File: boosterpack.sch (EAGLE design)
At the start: 27 parts, among them J1 POWERPOLE_DOUBLE

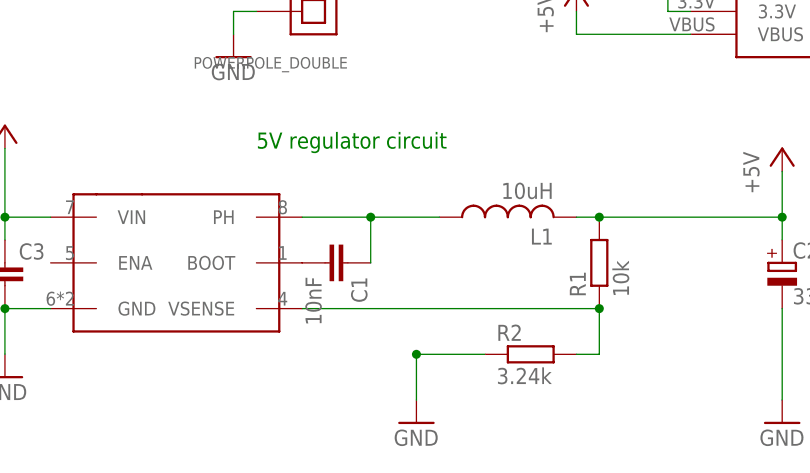
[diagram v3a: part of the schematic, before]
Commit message: added diode i forgot; routed new diode
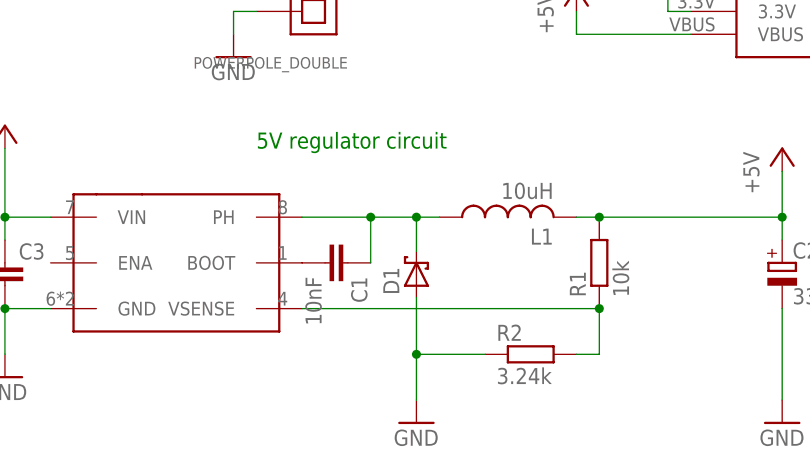
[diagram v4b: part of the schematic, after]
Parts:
- added D1: (no value), diode:SCHOTTKY-DIODEDO35-7
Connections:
- net GND: now also D1.A
- net N$11: now also D1.C
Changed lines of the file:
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@@
 <part name="GND7" library="supply1" deviceset="GND" device=""/>
 <part name="GND8" library="supply1" deviceset="GND" device=""/>
+<part name="D1" library="diode" deviceset="SCHOTTKY-DIODE" device="DO35-7"/>
 </parts>
 <sheets>
@@
 <instance part="GND7" gate="1" x="134.62" y="86.36"/>
 <instance part="GND8" gate="1" x="-2.54" y="73.66"/>
+<instance part="D1" gate="G$1" x="25.4" y="-3.81" rot="R90"/>
 </instances>
 <busses>
@@
 <wire x1="25.4" y1="-12.7" x2="25.4" y2="-17.78" width="0.1524" layer="91"/>
 <junction x="25.4" y="-12.7"/>
+<pinref part="D1" gate="G$1" pin="A"/>
+<wire x1="25.4" y1="-12.7" x2="25.4" y2="-6.35" width="0.1524" layer="91"/>
 </segment>
 <segment>
@@
 <wire x1="12.7" y1="2.54" x2="20.32" y2="2.54" width="0.1524" layer="91"/>
 <pinref part="C1" gate="G$1" pin="1"/>
-<wire x1="20.32" y1="2.54" x2="27.94" y2="2.54" width="0.1524" layer="91"/>
+<wire x1="20.32" y1="2.54" x2="25.4" y2="2.54" width="0.1524" layer="91"/>
+<wire x1="25.4" y1="2.54" x2="27.94" y2="2.54" width="0.1524" layer="91"/>
 <wire x1="20.32" y1="-2.54" x2="20.32" y2="2.54" width="0.1524" layer="91"/>
 <junction x="20.32" y="2.54"/>
-</segment>
-</net>
+<pinref part="D1" gate="G$1" pin="C"/>
+<wire x1="25.4" y1="-1.27" x2="25.4" y2="2.54" width="0.1524" layer="91"/>
+<junction x="25.4" y="2.54"/>
+</segment>
+</net>

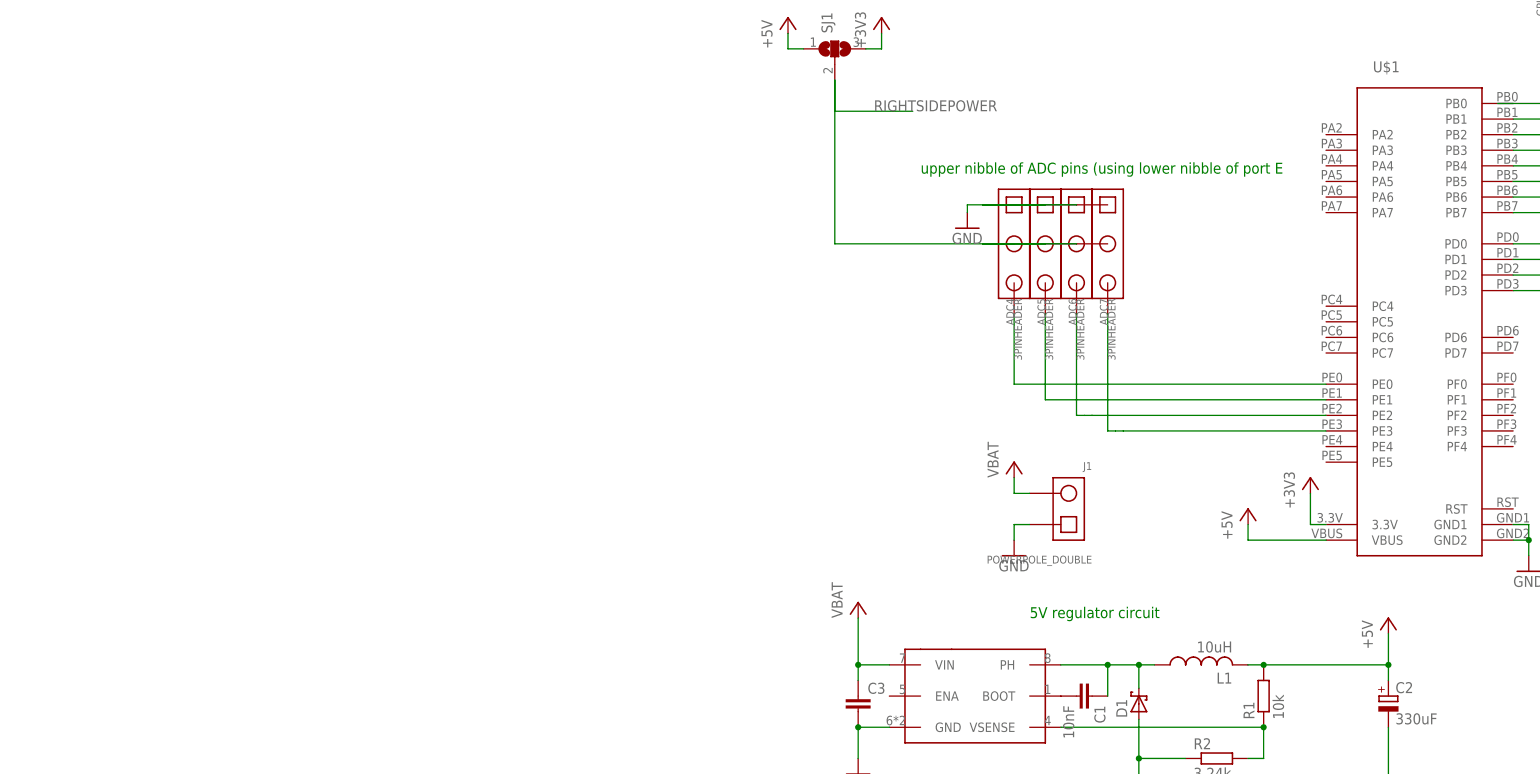
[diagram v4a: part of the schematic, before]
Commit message: added spi motor driver for two motors
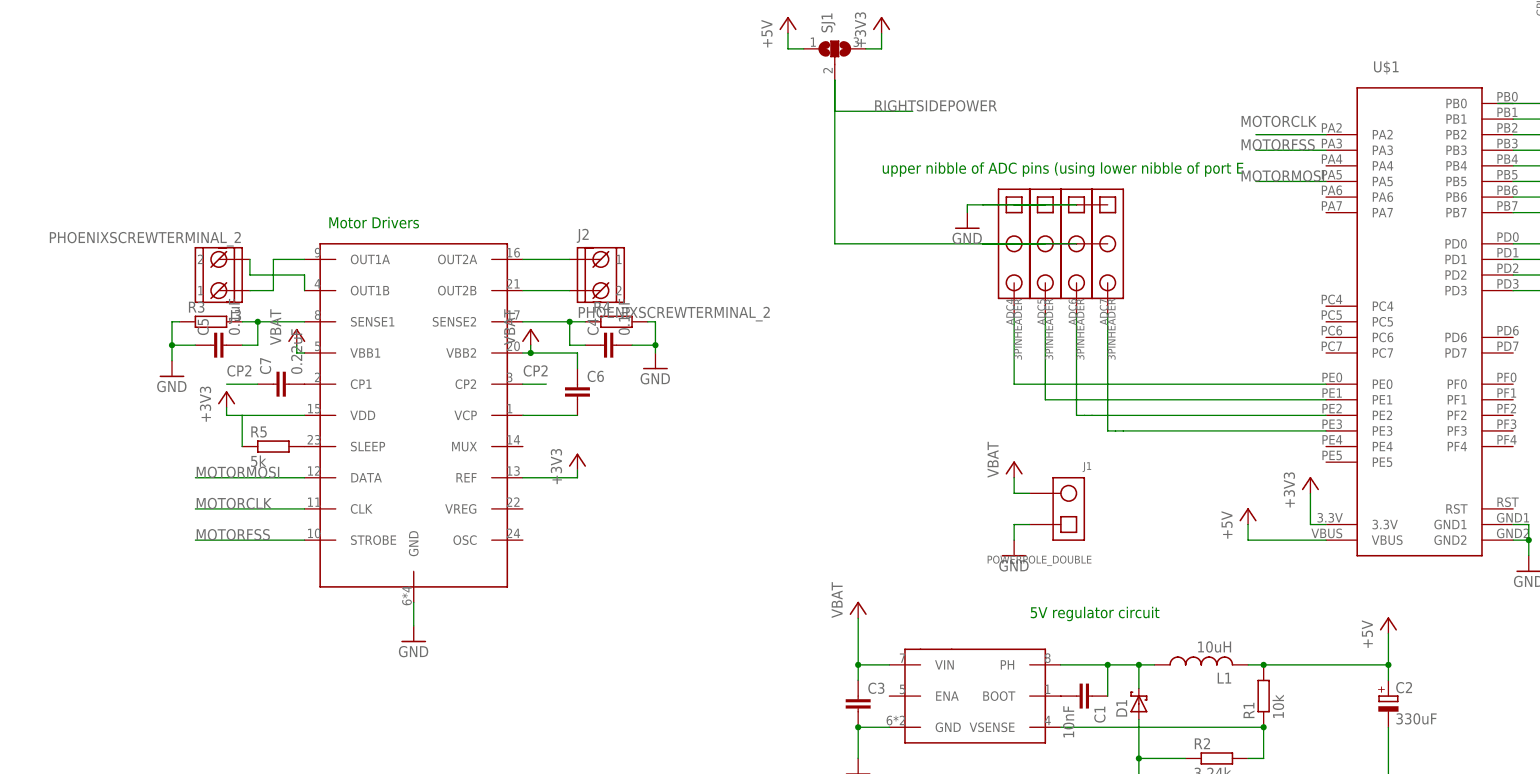
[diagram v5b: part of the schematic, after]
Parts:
- added C4, C5: 0.1uF, resistor:C-EU025-025X050
- added C6: (no value), resistor:C-EU025-025X050
- added C7: 0.22uF, resistor:C-EU025-024X044
- added J2, J3: PHOENIXSCREWTERMINAL_2, RASEagleLib:PHOENIXSCREWTERMINAL_2
- added R3, R4: (no value), resistor:R-EU_0204/5
- added R5: 5k, resistor:R-EU_0204/5
- added U$3: A3992A, RASEagleLib:A3992A
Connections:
- new net +3V3: R5.1, U$3.REF, U$3.VDD
- new net CP2: C7.1, U$3.CP2
- new net MOTORCLK: U$1.PA2, U$3.CLK
- new net MOTORFSS: U$1.PA3, U$3.STROBE
- new net MOTORMOSI: U$1.PA5, U$3.DATA
- new net N$14: J3.2, U$3.OUT1B
- new net N$15: J3.1, U$3.OUT1A
- new net N$17: J2.1, U$3.OUT2A
- new net N$18: J2.2, U$3.OUT2B
- new net N$19: C5.2, R3.2, U$3.SENSE1
- new net N$20: C4.1, R4.1, U$3.SENSE2
- new net N$21: C6.2, U$3.VCP
- new net N$22: R5.2, U$3.SLEEP
- new net N$23: C7.2, U$3.CP1
- net GND: now also C4.2, C5.1, R3.1, R4.2, U$3.GND
- net VCC: now also C6.1, U$3.VBB1, U$3.VBB2
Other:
- note added: "Motor Drivers"

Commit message: fixed 3v3 not connecting to the motor drivers and rerouted some stuff
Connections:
- removed net N$16: SJ1.3, SJ2.3, U$1.3.3V
- net +3V3: now also SJ1.3, SJ2.3, U$1.3.3V
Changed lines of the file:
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@@
-</segment>
-</net>
-<net name="N$16" class="0">
-<segment>
-<pinref part="SJ2" gate="G$1" pin="3"/>
-<pinref part="+3V2" gate="G$1" pin="+3V3"/>
-<wire x1="73.66" y1="129.54" x2="76.2" y2="129.54" width="0.1524" layer="91"/>
-<wire x1="76.2" y1="129.54" x2="76.2" y2="132.08" width="0.1524" layer="91"/>
-</segment>
-<segment>
-<pinref part="U$1" gate="G$1" pin="3.3V"/>
-<pinref part="+3V3" gate="G$1" pin="+3V3"/>
-<wire x1="55.88" y1="25.4" x2="53.34" y2="25.4" width="0.1524" layer="91"/>
-<wire x1="53.34" y1="25.4" x2="53.34" y2="30.48" width="0.1524" layer="91"/>
-</segment>
-<segment>
-<pinref part="SJ1" gate="G$1" pin="3"/>
-<pinref part="+3V1" gate="G$1" pin="+3V3"/>
-<wire x1="-19.05" y1="102.87" x2="-16.51" y2="102.87" width="0.1524" layer="91"/>
-<wire x1="-16.51" y1="102.87" x2="-16.51" y2="105.41" width="0.1524" layer="91"/>
 </segment>
 </net>
@@
 <wire x1="-66.04" y1="33.02" x2="-66.04" y2="34.29" width="0.1524" layer="91"/>
 </segment>
+<segment>
+<pinref part="SJ2" gate="G$1" pin="3"/>
+<pinref part="+3V2" gate="G$1" pin="+3V3"/>
+<wire x1="73.66" y1="129.54" x2="76.2" y2="129.54" width="0.1524" layer="91"/>
+<wire x1="76.2" y1="129.54" x2="76.2" y2="132.08" width="0.1524" layer="91"/>
+</segment>
+<segment>
+<pinref part="U$1" gate="G$1" pin="3.3V"/>
+<pinref part="+3V3" gate="G$1" pin="+3V3"/>
+<wire x1="55.88" y1="25.4" x2="53.34" y2="25.4" width="0.1524" layer="91"/>
+<wire x1="53.34" y1="25.4" x2="53.34" y2="30.48" width="0.1524" layer="91"/>
+</segment>
+<segment>
+<pinref part="SJ1" gate="G$1" pin="3"/>
+<pinref part="+3V1" gate="G$1" pin="+3V3"/>
+<wire x1="-19.05" y1="102.87" x2="-16.51" y2="102.87" width="0.1524" layer="91"/>
+<wire x1="-16.51" y1="102.87" x2="-16.51" y2="105.41" width="0.1524" layer="91"/>
+</segment>
 </net>

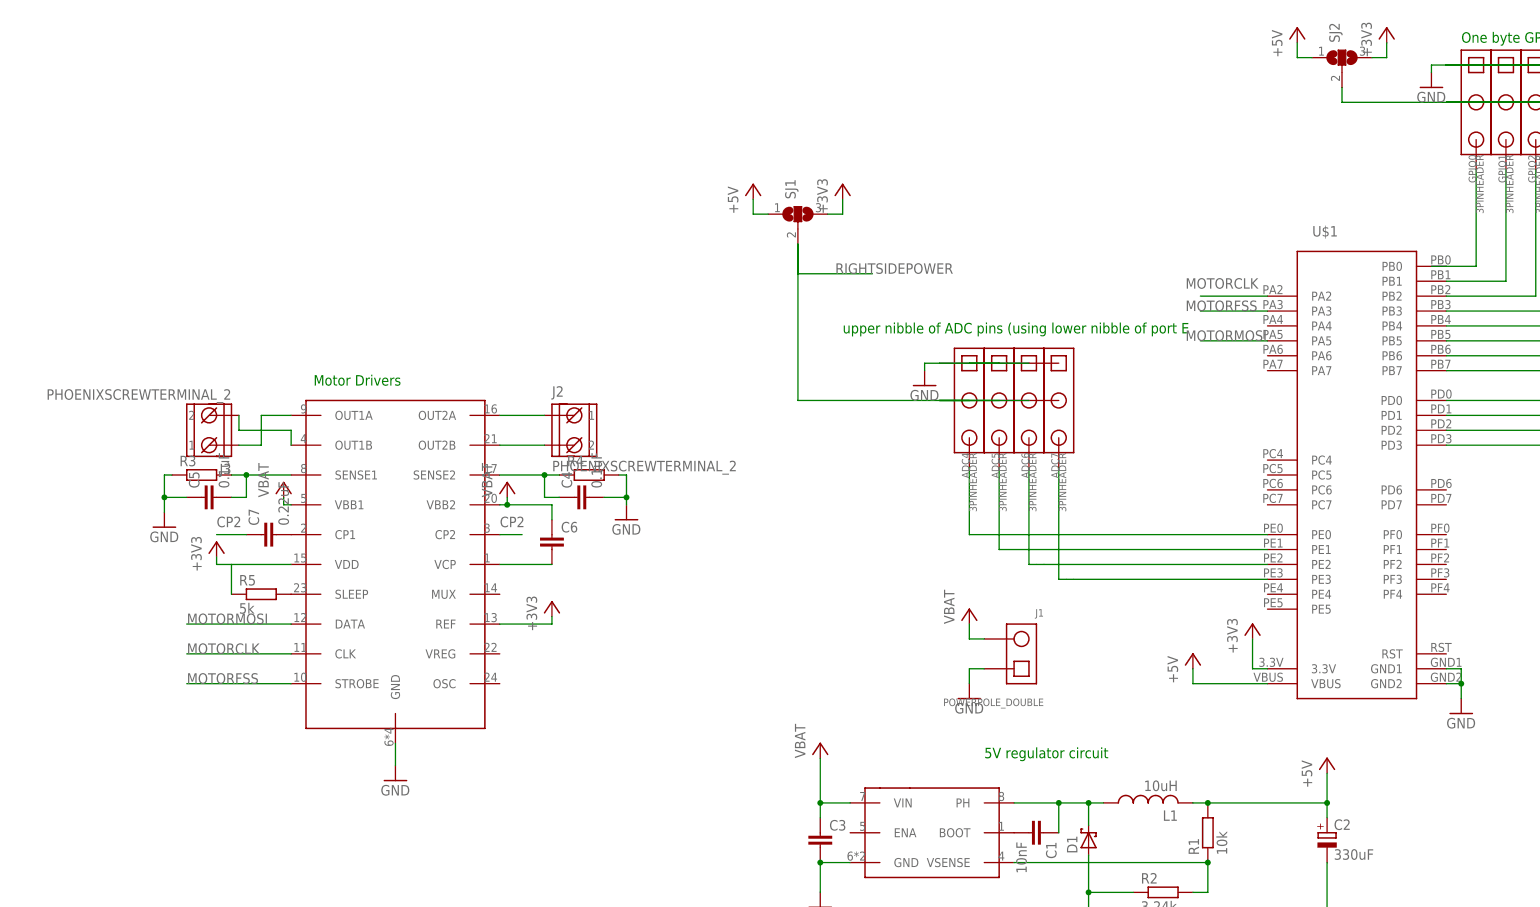
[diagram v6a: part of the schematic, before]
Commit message: Removed motor drivers, almost done wiring board
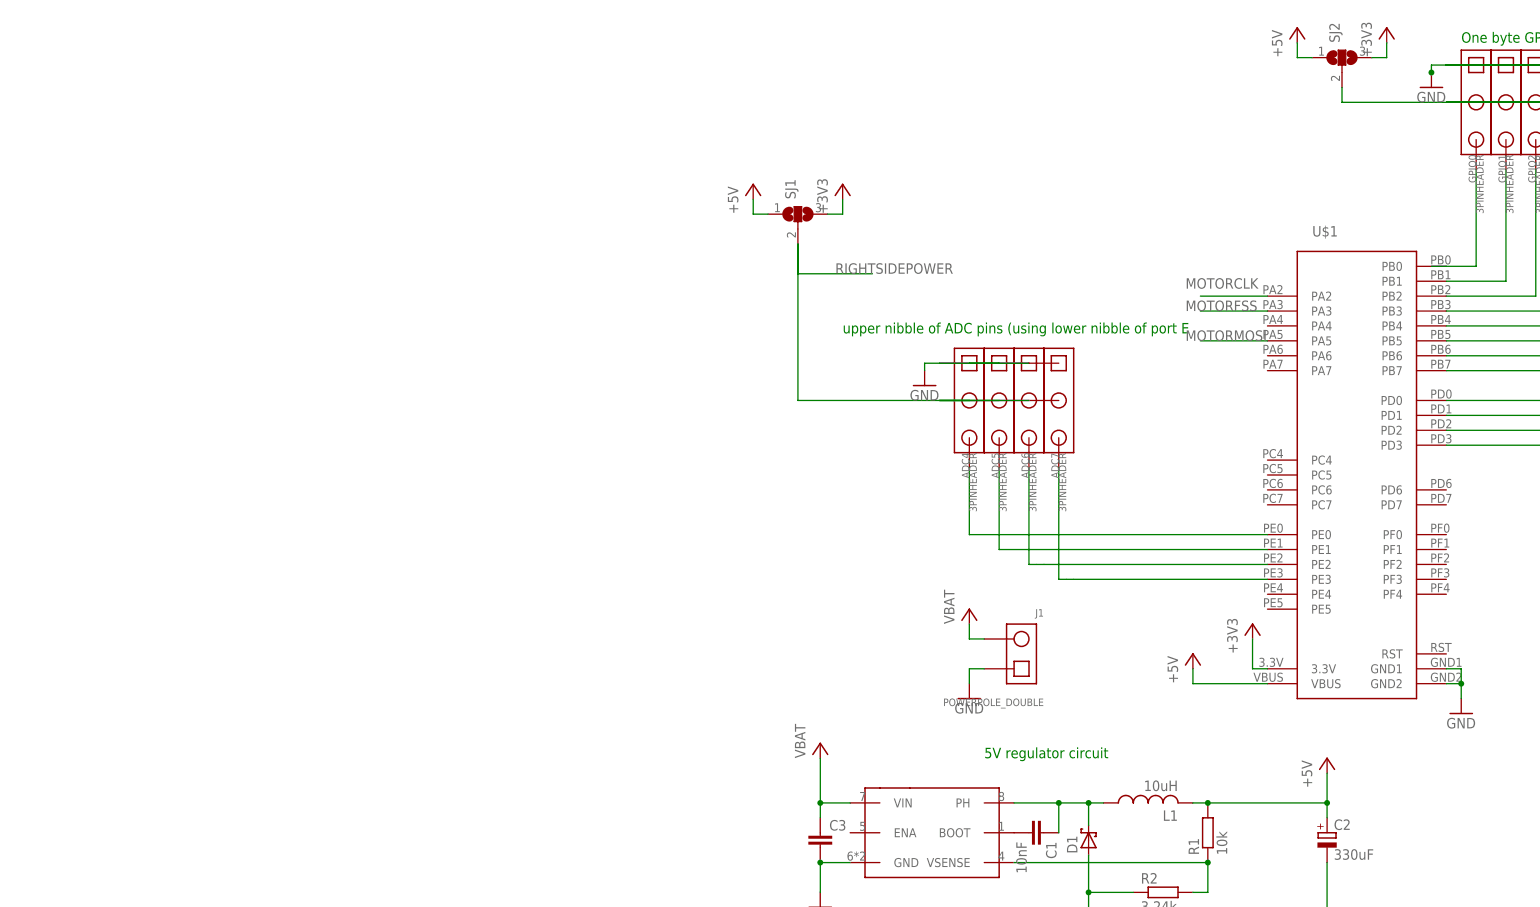
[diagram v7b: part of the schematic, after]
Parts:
- removed C4, C5: 0.1uF, resistor:C-EU025-025X050
- removed C6: (no value), resistor:C-EU025-025X050
- removed C7: 0.22uF, resistor:C-EU025-024X044
- removed J2, J3: PHOENIXSCREWTERMINAL_2, RASEagleLib:PHOENIXSCREWTERMINAL_2
- removed R3, R4: (no value), resistor:R-EU_0204/5
- removed R5: 5k, resistor:R-EU_0204/5
- removed U$3: A3992A, RASEagleLib:A3992A
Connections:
- removed net CP2: C7.1, U$3.CP2
- removed net N$14: J3.2, U$3.OUT1B
- removed net N$15: J3.1, U$3.OUT1A
- removed net N$17: J2.1, U$3.OUT2A
- removed net N$18: J2.2, U$3.OUT2B
- removed net N$19: C5.2, R3.2, U$3.SENSE1
- removed net N$20: C4.1, R4.1, U$3.SENSE2
- removed net N$21: C6.2, U$3.VCP
- removed net N$22: R5.2, U$3.SLEEP
- removed net N$23: C7.2, U$3.CP1
- net +3V3: no longer R5.1, U$3.REF, U$3.VDD
- net GND: no longer C4.2, C5.1, R3.1, R4.2, U$3.GND
- net MOTORCLK: no longer U$3.CLK
- net MOTORFSS: no longer U$3.STROBE
- net MOTORMOSI: no longer U$3.DATA
- net VCC: no longer C6.1, U$3.VBB1, U$3.VBB2
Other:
- note removed: "Motor Drivers"
